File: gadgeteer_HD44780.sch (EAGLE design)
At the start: 7 parts, among them T1 3904

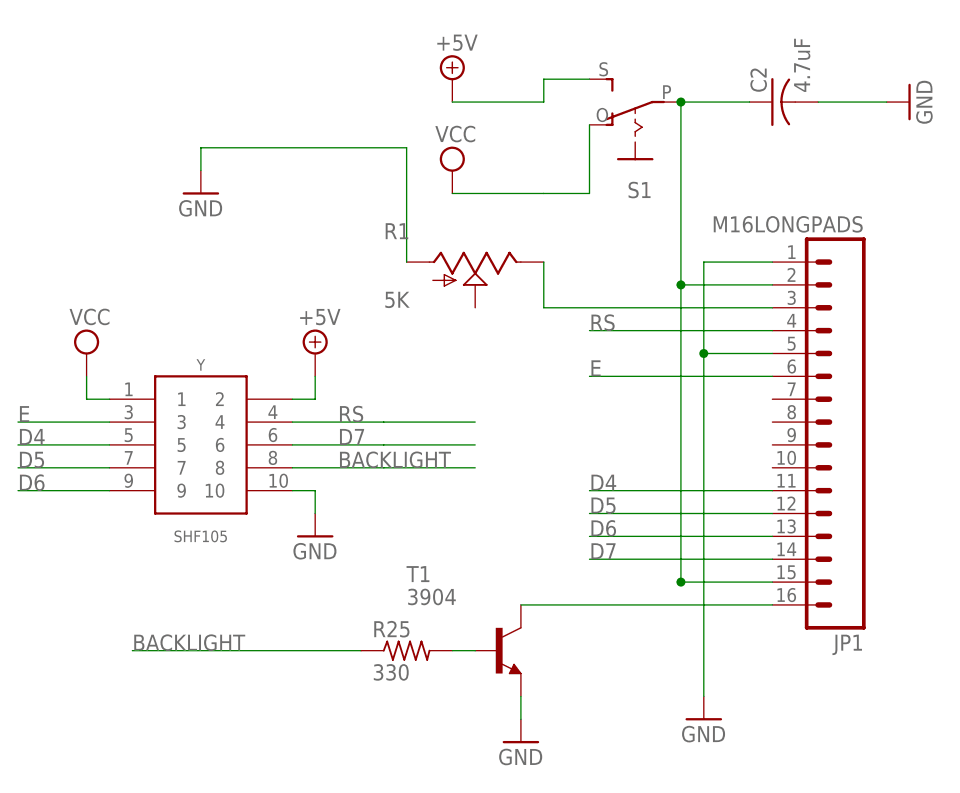
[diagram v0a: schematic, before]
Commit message: [FIX] Changed C1 to 1206K (Kemet) metric size
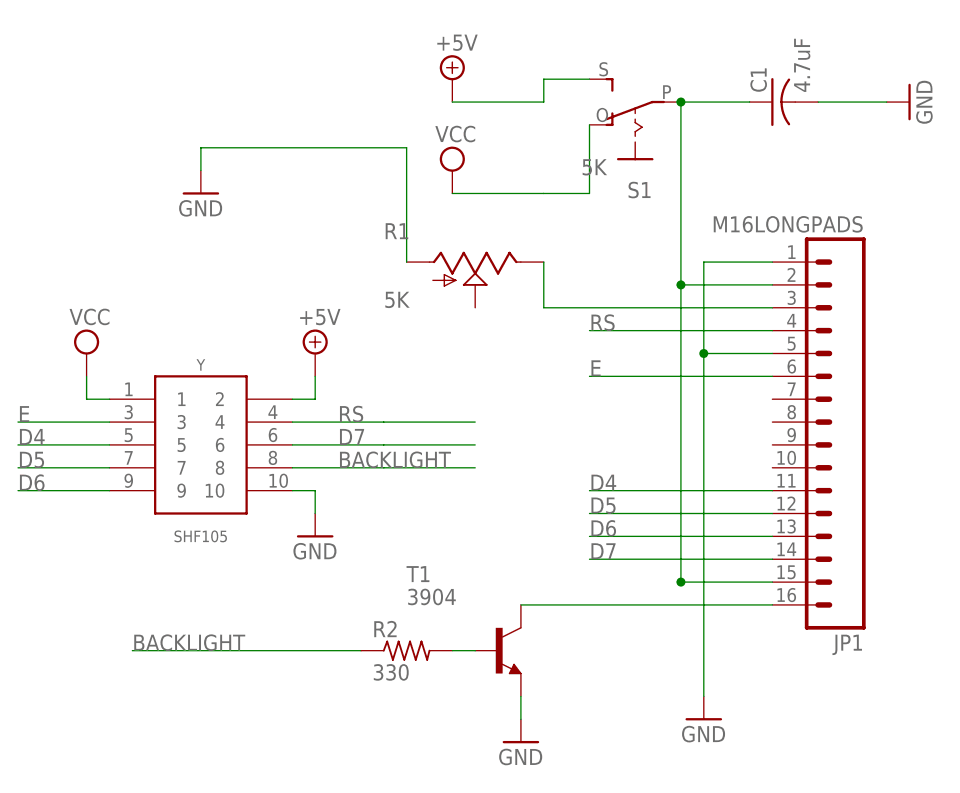
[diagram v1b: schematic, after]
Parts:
- removed C2: 4.7uF, adafruit:C-USC1206
- added C1: 4.7uF, adafruit:C-USC1206K
- S1: value (none) -> 5K
- renumbered R25 to R2
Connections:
- net GND: now also C1.2; no longer C2.2
- net N$2: now also C1.1; no longer C2.1
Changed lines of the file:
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@@
 <part name="JP1" library="SparkFun-Connectors" deviceset="M16" device="LONGPADS"/>
 <part name="SUPPLY3" library="supply2" deviceset="VCC" device=""/>
-<part name="C2" library="adafruit" deviceset="C-US" device="C1206" value="4.7uF"/>
 <part name="GND4" library="supply1" deviceset="GND" device=""/>
-<part name="R25" library="adafruit" deviceset="R-US_" device="R0603" value="330"/>
+<part name="R2" library="adafruit" deviceset="R-US_" device="R0603" value="330"/>
 <part name="T1" library="transistor" deviceset="*-NPN-" device="SOT23-BEC" technology="MMBT3904LT1" value="3904"/>
 <part name="Y" library="ozlollc" deviceset="SHF105" device=""/>
 <part name="SUPPLY4" library="supply2" deviceset="VCC" device=""/>
 <part name="GND5" library="supply1" deviceset="GND" device=""/>
-<part name="S1" library="adafruit" deviceset="EG1218" device="S"/>
+<part name="S1" library="adafruit" deviceset="EG1218" device="S" value="5K"/>
+<part name="C1" library="adafruit" deviceset="C-US" device="C1206K" value="4.7uF"/>
 </parts>
 <sheets>
@@
 <instance part="JP1" gate="G$1" x="99.06" y="48.26" rot="R180"/>
 <instance part="SUPPLY3" gate="G$1" x="53.34" y="78.74"/>
-<instance part="C2" gate="G$1" x="88.9" y="86.36" rot="R90"/>
 <instance part="GND4" gate="1" x="104.14" y="86.36" rot="R90"/>
-<instance part="R25" gate="G$1" x="48.26" y="25.4"/>
+<instance part="R2" gate="G$1" x="48.26" y="25.4"/>
 <instance part="T1" gate="G$1" x="58.42" y="25.4"/>
 <instance part="Y" gate="X" x="25.4" y="48.26"/>
@@
 <instance part="GND5" gate="1" x="25.4" y="76.2"/>
 <instance part="S1" gate="1" x="73.66" y="83.82" rot="R90"/>
+<instance part="C1" gate="G$1" x="88.9" y="86.36" rot="R90"/>
 </instances>
 <busses>
@@
 </segment>
 <segment>
-<pinref part="C2" gate="G$1" pin="2"/>
 <pinref part="GND4" gate="1" pin="GND"/>
 <wire x1="93.98" y1="86.36" x2="101.6" y2="86.36" width="0.1524" layer="91"/>
+<pinref part="C1" gate="G$1" pin="2"/>
 </segment>
 <segment>
@@
 <pinref part="JP1" gate="G$1" pin="2"/>
 <wire x1="78.74" y1="66.04" x2="88.9" y2="66.04" width="0.1524" layer="91"/>
-<pinref part="C2" gate="G$1" pin="1"/>
 <wire x1="78.74" y1="86.36" x2="86.36" y2="86.36" width="0.1524" layer="91"/>
 <junction x="78.74" y="66.04"/>
@@
 <pinref part="S1" gate="1" pin="P"/>
 <junction x="78.74" y="86.36"/>
+<pinref part="C1" gate="G$1" pin="1"/>
 </segment>
 </net>
 <net name="N$3" class="0">
 <segment>
-<pinref part="R25" gate="G$1" pin="2"/>
+<pinref part="R2" gate="G$1" pin="2"/>
 <pinref part="T1" gate="G$1" pin="B"/>
 <wire x1="53.34" y1="25.4" x2="55.88" y2="25.4" width="0.1524" layer="91"/>
@@
 <net name="BACKLIGHT" class="0">
 <segment>
-<pinref part="R25" gate="G$1" pin="1"/>
+<pinref part="R2" gate="G$1" pin="1"/>
 <wire x1="43.18" y1="25.4" x2="17.78" y2="25.4" width="0.1524" layer="91"/>
 <label x="17.78" y="25.4" size="1.778" layer="95"/>
